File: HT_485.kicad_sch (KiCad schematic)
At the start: 80 parts, among them J1 POWER, J2 485, J3 PT1000, J4 H/T Sensor, J5 PRG, Q1 BC817, Q2 BC817, Q3 BC817, Q4 BC817, U1 MAX14786EAUD+T, U2 TL082, U3 LM2576D2TR4-3.3G, U4 ESP32-S3-WROOM-1-N16R8, U6 L7815

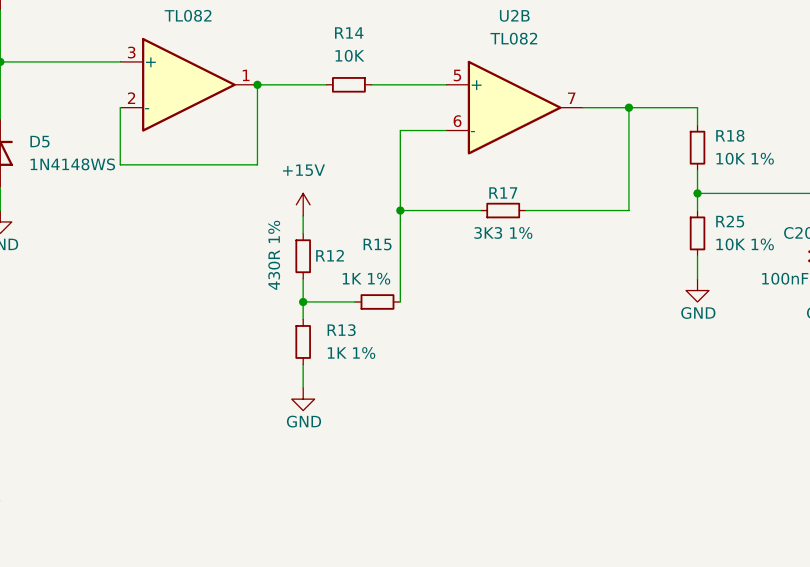
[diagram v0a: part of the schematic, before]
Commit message: Provato cambio resistenze operazionali. NULLA
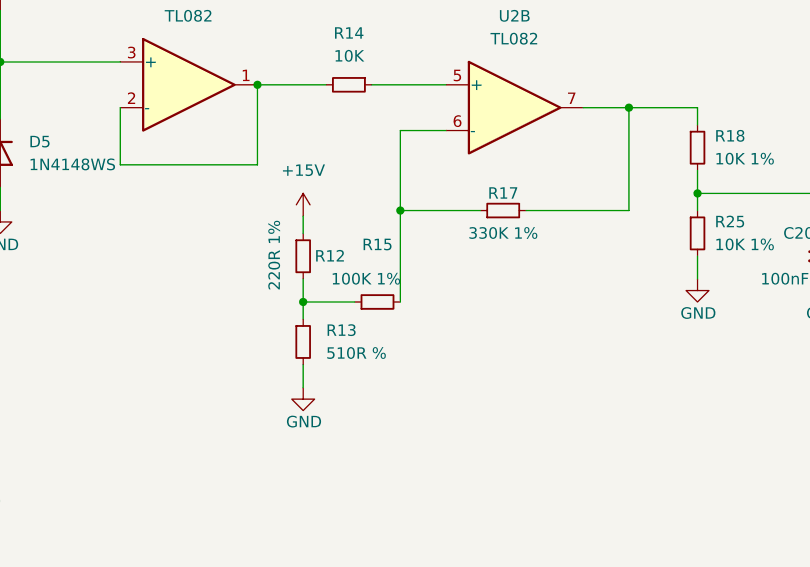
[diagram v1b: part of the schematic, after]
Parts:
- R12: value 430R 1% -> 220R 1%
- R13: value 1K 1% -> 510R %
- R15: value 1K 1% -> 100K 1%
- R17: value 3K3 1% -> 330K 1%
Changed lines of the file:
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@@
     (in_bom yes) (on_board yes)
     (property "Reference" "R17" (id 0) (at 109.855 201.295 90))
-    (property "Value" "3K3 1%" (id 1) (at 109.855 205.74 90))
+    (property "Value" "330K 1%" (id 1) (at 109.855 205.74 90))
     (property "Footprint" "Resistor_SMD:R_0805_2012Metric_Pad1.20x1.40mm_HandSolder" (id 2) (at 109.855 203.2 0)
       (effects (font (size 1.27 1.27)) hide)
@@
       (effects (font (size 1.27 1.27)) (justify left))
     )
-    (property "Value" "430R 1%" (id 1) (at 84.455 212.09 90)
+    (property "Value" "220R 1%" (id 1) (at 84.455 212.09 90)
       (effects (font (size 1.27 1.27)) (justify left))
     )
@@
       (effects (font (size 1.27 1.27)) (justify left))
     )
-    (property "Value" "1K 1%" (id 1) (at 90.17 219.0749 0)
+    (property "Value" "510R %" (id 1) (at 90.17 219.0749 0)
       (effects (font (size 1.27 1.27)) (justify left))
     )
@@
     (in_bom yes) (on_board yes)
     (property "Reference" "R15" (id 0) (at 95.885 207.01 90))
-    (property "Value" "1K 1%" (id 1) (at 94.615 210.82 90))
+    (property "Value" "100K 1%" (id 1) (at 94.615 210.82 90))
     (property "Footprint" "Resistor_SMD:R_0805_2012Metric_Pad1.20x1.40mm_HandSolder" (id 2) (at 95.885 213.36 0)
       (effects (font (size 1.27 1.27)) hide)
@@
     )
     (path "/37a4da1b-b23e-4c99-92c5-1edd1e260509"
-      (reference "R12") (unit 1) (value "430R 1%") (footprint "Resistor_SMD:R_0805_2012Metric_Pad1.20x1.40mm_HandSolder")
+      (reference "R12") (unit 1) (value "220R 1%") (footprint "Resistor_SMD:R_0805_2012Metric_Pad1.20x1.40mm_HandSolder")
     )
     (path "/9b2c5abb-3c78-49d8-8ccb-d7a77fc4039f"
-      (reference "R13") (unit 1) (value "1K 1%") (footprint "Resistor_SMD:R_0805_2012Metric_Pad1.20x1.40mm_HandSolder")
+      (reference "R13") (unit 1) (value "510R %") (footprint "Resistor_SMD:R_0805_2012Metric_Pad1.20x1.40mm_HandSolder")
     )
     (path "/c2ad6d7a-43e9-4769-ab7d-5b48aedd331e"
@@
     )
     (path "/dafc20e6-5160-4991-b11c-f4df07558de3"
-      (reference "R15") (unit 1) (value "1K 1%") (footprint "Resistor_SMD:R_0805_2012Metric_Pad1.20x1.40mm_HandSolder")
+      (reference "R15") (unit 1) (value "100K 1%") (footprint "Resistor_SMD:R_0805_2012Metric_Pad1.20x1.40mm_HandSolder")
     )
     (path "/c722abe2-39f6-4182-8f35-73ac3a447bdd"
@@
     )
     (path "/2ea8c421-e022-4b53-ab9d-747574ed23fe"
-      (reference "R17") (unit 1) (value "3K3 1%") (footprint "Resistor_SMD:R_0805_2012Metric_Pad1.20x1.40mm_HandSolder")
+      (reference "R17") (unit 1) (value "330K 1%") (footprint "Resistor_SMD:R_0805_2012Metric_Pad1.20x1.40mm_HandSolder")
     )
     (path "/7ce32af9-e8f8-4200-8b4f-d83e817f1fc3"

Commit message: Ancora problemi PT1000
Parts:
- R13: value 510R % -> 220R 1%
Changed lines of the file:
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@@
       (effects (font (size 1.27 1.27)) (justify left))
     )
-    (property "Value" "510R %" (id 1) (at 90.17 219.0749 0)
+    (property "Value" "220R 1%" (id 1) (at 90.17 219.0749 0)
       (effects (font (size 1.27 1.27)) (justify left))
     )
@@
     )
     (path "/9b2c5abb-3c78-49d8-8ccb-d7a77fc4039f"
-      (reference "R13") (unit 1) (value "510R %") (footprint "Resistor_SMD:R_0805_2012Metric_Pad1.20x1.40mm_HandSolder")
+      (reference "R13") (unit 1) (value "220R 1%") (footprint "Resistor_SMD:R_0805_2012Metric_Pad1.20x1.40mm_HandSolder")
     )
     (path "/c2ad6d7a-43e9-4769-ab7d-5b48aedd331e"

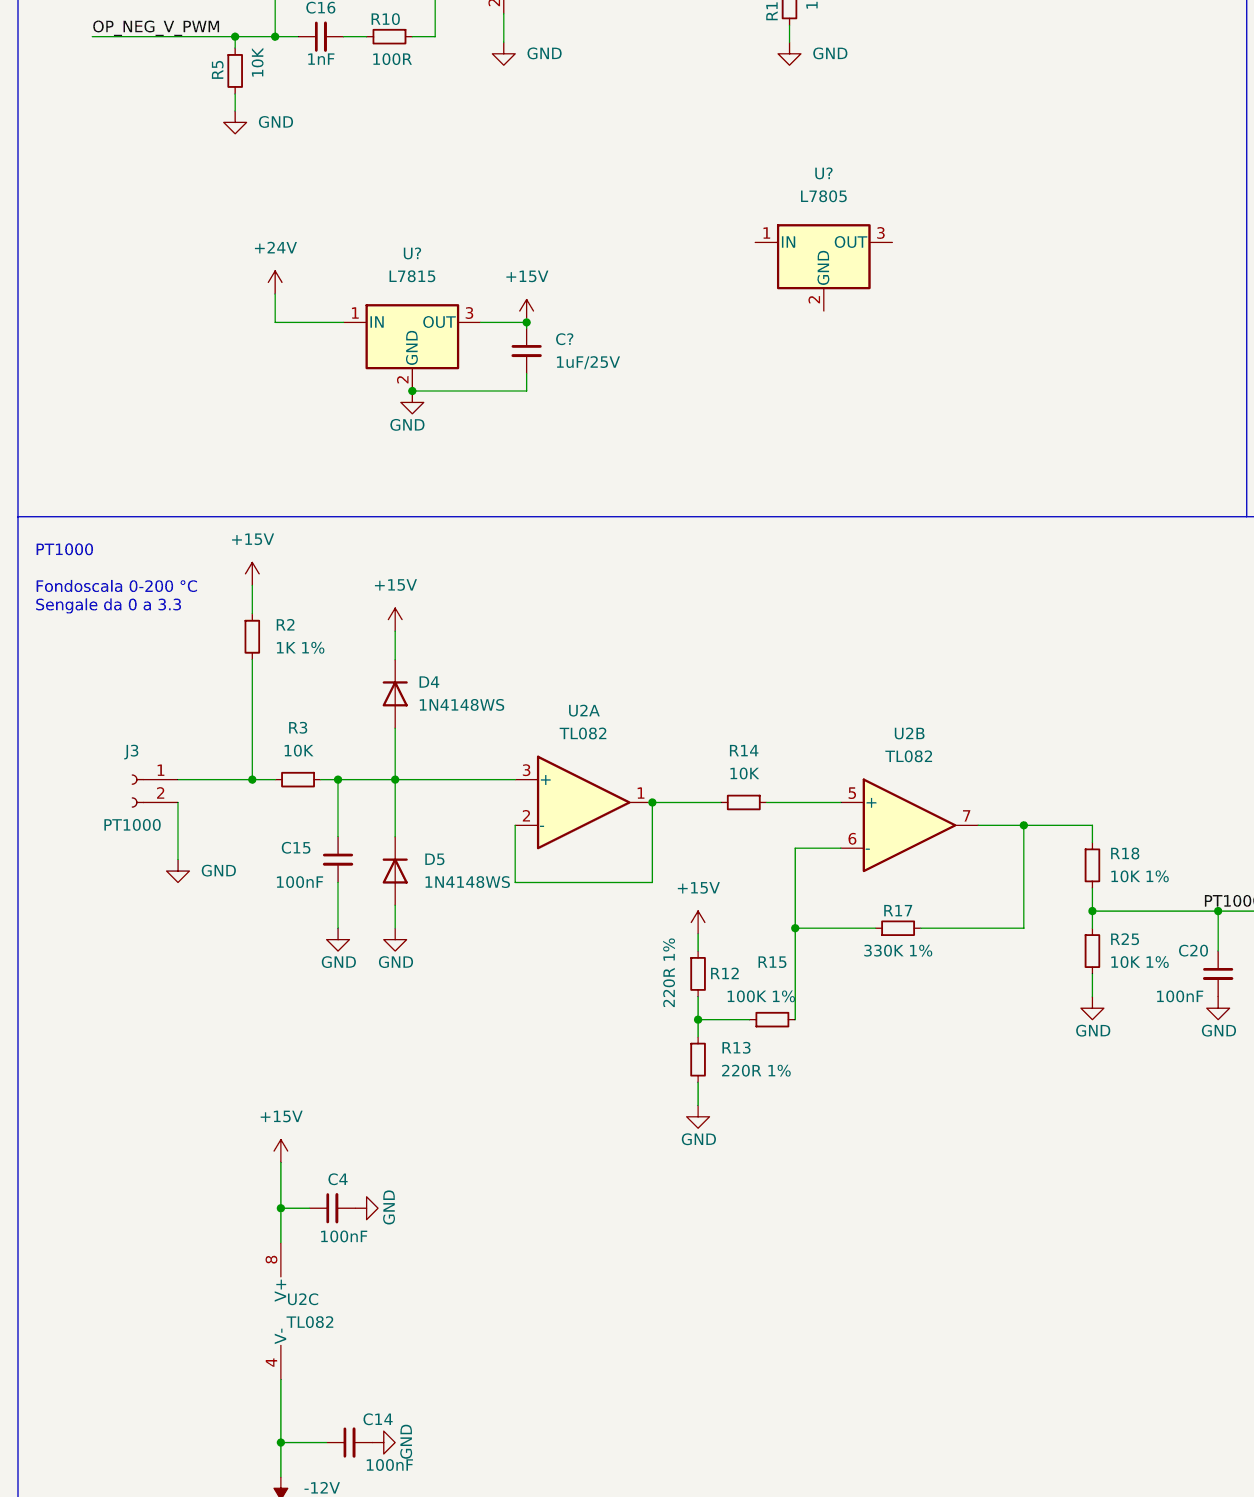
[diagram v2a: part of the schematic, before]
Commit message: Rivisto completamente PT1000 ingresso
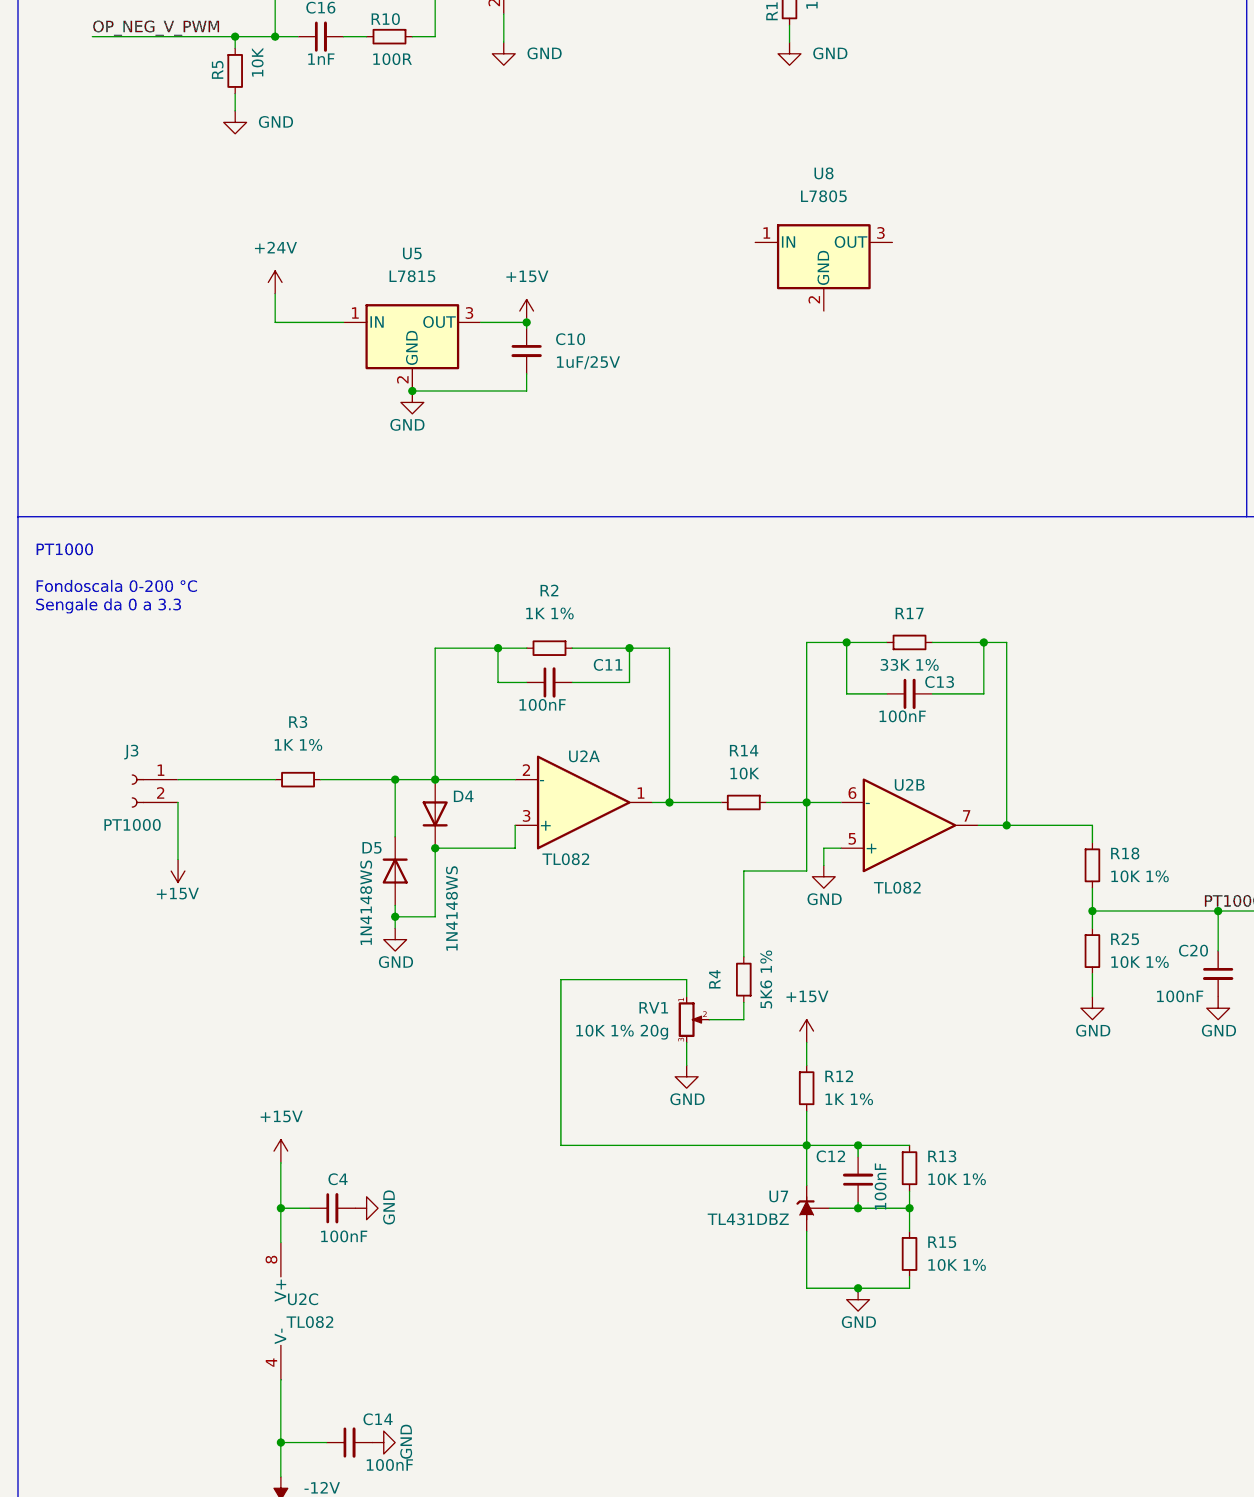
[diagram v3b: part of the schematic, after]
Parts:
- removed C15: 100nF, Capacitor_SMD:C_0805_2012Metric, symbol Device:C_Small
- added C11, C12, C13: 100nF, Capacitor_SMD:C_0805_2012Metric, symbol Device:C_Small
- added R4: 5K6 1%, Resistor_SMD:R_0805_2012Metric_Pad1.20x1.40mm_HandSolder, symbol Device:R_Small
- added RV1: 10K 1% 20g, symbol Device:R_Potentiometer_Small
- added U7: TL431DBZ, Package_TO_SOT_SMD:SOT-23, symbol Reference_Voltage:TL431DBZ
- R12: value 220R 1% -> 1K 1%
- R13: value 220R 1% -> 10K 1%
- R15: value 100K 1% -> 10K 1%
- R17: value 330K 1% -> 33K 1%
- R3: value 10K -> 1K 1%
- gave numbers to parts that had none: 3
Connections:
- net +15V: now also J3.2 (Pin_2); no longer D4.1 (K), R2.1
- net GND: now also D4.1 (K), R15.2, U2.3 (+), U2.5 (+), RV1.3, U7.3 (A); no longer J3.2 (Pin_2), R13.2
- net at R14.1: now also R17.1, U2.6 (-), C13.1, R4.2; no longer U2.5 (+)
- net at R17.2, R18.1, U2.7: now also C13.2
- net at R12.2, R13.1: now also C12.2, RV1.1, U7.1 (K); no longer R15.1
- net at J3.1 (Pin_1), R3.2: no longer R2.2
- net at R14.2, U2.1: now also R2.1, C11.2; no longer U2.2 (-)
- net at D4.2 (A), D5.1 (K), R3.1: now also R2.2, U2.2 (-), C11.1; no longer U2.3 (+)
- new net: R4.1, RV1.2
- new net: C12.1, R13.2, R15.1, U7.2 (REF)
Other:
- moved on the sheet: D4, R17

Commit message: Rifatto schema 485. Master da rifare
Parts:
- removed C7: 1000uF/10V, Capacitor_SMD:CP_Elec_10x10.5, symbol Device:C_Polarized_Small
- removed D10: STPS0520Z, Diode_SMD:D_SOD-123, symbol Device:D_Schottky_Small
- removed D2: 3.9V/1W, Diode_SMD:D_SMA, symbol Device:D_Zener_Small
- removed JP2: BIAS-, Jumper:SolderJumper-2_P1.3mm_Open_RoundedPad1.0x1.5mm, symbol Jumper:SolderJumper_2_Open
- removed JP4: UART_BOOT_MSG, Jumper:SolderJumper-3_P1.3mm_Bridged12_RoundedPad1.0x1.5mm_NumberLabels, symbol Jumper:SolderJumper_3_Bridged12
- removed U1: MAX14786EAUD+T, Package_SO:SOIC-8_3.9x4.9mm_P1.27mm, symbol Interface_UART:MAX485E
- removed U3: LM2576D2TR4-3.3G, Package_TO_SOT_SMD:TO-263-5_TabPin3, symbol Regulator_Switching:LM2575-3.3BU
- removed U5: L7815, Package_TO_SOT_SMD:TO-263-2, symbol Regulator_Linear:L7815
- removed U8: L7805, Package_TO_SOT_SMD:TO-263-2, symbol Regulator_Linear:L7805
- added C15: 1000uF/25V, Capacitor_THT:CP_Radial_D10.0mm_P2.50mm_P5.00mm, symbol Device:C_Polarized_Small
- added C21: 1uF / 25V, Capacitor_SMD:C_0805_2012Metric, symbol Device:C_Small
- added C22, C23: 4.7uF, Capacitor_SMD:C_0805_2012Metric, symbol Device:C_Small
- added C24, C25: 100nF, Capacitor_SMD:C_0805_2012Metric, symbol Device:C_Small
- added C7: 10uF / 25V, Capacitor_SMD:C_0805_2012Metric, symbol Device:C_Small
- added D10, D11, D12, D13, D14, D2: BAR43SFILM, Package_TO_SOT_SMD:SOT-23, symbol Device:D_Dual_Series_AKC
- added Q10, Q5, Q6, Q7, Q8, Q9: BS170, Package_TO_SOT_SMD:SOT-23, symbol Transistor_FET:BS170
- added R32, R33, R34, R35, R36, R37, R41, R42, R43, R44, R45, R46: 4K7, Resistor_SMD:R_0805_2012Metric_Pad1.20x1.40mm_HandSolder, symbol Device:R_Small
- added R38, R39, R40: 10R, Resistor_SMD:R_0805_2012Metric_Pad1.20x1.40mm_HandSolder, symbol Device:R_Small
- added R47: 120R, Resistor_SMD:R_0805_2012Metric_Pad1.20x1.40mm_HandSolder, symbol Device:R_Small
- added SW1: 485_PWR_1, Connector_PinHeader_2.54mm:PinHeader_1x03_P2.54mm_Vertical, symbol Switch:SW_SPDT
- added SW2: 485_PWR_2, Connector_PinHeader_2.54mm:PinHeader_1x03_P2.54mm_Vertical, symbol Switch:SW_SPDT
- added U1: L7805, Package_TO_SOT_SMD:TO-252-3_TabPin2, symbol Regulator_Linear:L7805
- added U3: LD1086DT33TR, Package_TO_SOT_SMD:TO-252-3_TabPin2, symbol Regulator_Linear:LD1117S33TR_SOT223
- added U5: LM2576S-12/NOPB, Package_TO_SOT_SMD:TO-263-5_TabPin3, symbol Regulator_Switching:LM2575-3.3BU
- added U8, U9: MAX485, Package_SO:SOIC-8_3.9x4.9mm_P1.27mm, symbol Interface_UART:MAX485E
- C1: value 4.7uF -> 10uF / 25V
- C10: value 1uF/25V -> 1nF/25V
- C2: value 100nF -> 10uF / 25V
- C5: value 100uF / 50V -> 100uF/75V; footprint Capacitor_SMD:CP_Elec_8x10.5 -> Capacitor_THT:CP_Radial_D10.0mm_P2.50mm_P5.00mm
- C6: value 1nF/10V -> 10uF / 25V
- J1: value POWER -> 485_1
- J2: value 485 -> 485_1
- JP1: value BIAS+ -> TERMINATOR
- L1: value 100uH -MSS1210-104KED -> MSS1210-104KED -100uH; footprint HT485:MSS1210-104KED -> SES:MSS1210-104KED
- R20: value 370R -> 0R
- R21: value 370R -> 10R
- R23: value 4K7 -> 10R
- R31: value 10K -> 10R
- U4: value ESP32-S3-WROOM-1-N16R8 -> ESP32-S3-WROOM-1U-N16R8
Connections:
- net +15V: no longer C10.1
- net +24V: now also U5.1 (VIN); no longer J1.2 (Pin_2)
- net +3V3: now also C7.1, D10.2 (K), D11.2 (K), D12.2 (K), D13.2 (K), D14.2 (K), D2.2 (K), Q10.2 (G), Q5.2 (G), Q6.2 (G), Q7.2 (G), Q8.2 (G), Q9.2 (G), R32.2, R33.2, R34.2, R41.2, R42.2, R43.2, U3.2 (VO); no longer L1.2, R20.1, R23.2, R31.1
- net +5V: now also C2.1, C6.1, SW1.3 (C), SW2.3 (C), U1.3 (OUT), U3.3 (VI); no longer C1.2, C2.2
- net GND: now also C1.2, C2.2, R1.1, C15.2, C21.2, C22.1, C23.1, C24.1, C25.1, C7.2, D10.1 (A), D11.1 (A), D12.1 (A), D13.1 (A), D14.1 (A), D2.1 (A), U1.2 (GND), U3.1 (GND), U5.5 (~{ON}/OFF), U8.5 (GND), U9.5 (GND); no longer C1.1, C2.1, J1.1 (Pin_1), R1.2, R21.2
- net at D1.1 (K), L1.1, R6.1: now also U5.2 (OUT)
- net at U4.16 (GPIO46): now also R30.1
- net DE2: now reaches U4.20 (GPIO12/TOUCH11/ADC2_CH0/FSPICS0/FSPIIO4/SUBSPICS0)
- net DE2: now also D14.3 (common), R40.2
- net TX2: now reaches U4.21 (GPIO13/TOUCH13/ADC2_CH2/FSPIQ/FSPIIO7/SUBSPIQ)
- net TX2: now also D13.3 (common), R39.2
- net RX2: now reaches U4.22 (GPIO14/TOUCH14/ADC2_CH3/FSPIWP/FSPIDQS/SUBSPIWP)
- net RX2: now also D12.3 (common), R38.2
- net DE1: now reaches U4.9 (GPIO16/U0CTS/ADC2_CH5/XTAL_32K_NH5)
- net DE1: now also R31.2, D11.3 (common)
- net at R6.2: now also C10.1; no longer C6.1
- net +12V: now reaches R20.2
- net +12V: now also C1.1, L1.2, C15.1, C21.1, SW1.1 (A), SW2.1 (A), U1.1 (IN); no longer JP1.2 (B)
- net at R21.1: now also Q5.3 (S), R32.1
- net 485+ renamed 485_1+
- net 485_1+: now also U9.7 (B); no longer JP1.1 (A)
- net 485- renamed 485_1-
- net 485_1-: now also U9.6 (A)
- net DE: no longer names the net of U4.4 (GPIO4/TOUCH4/ADC1_CH3)
- net DE: no longer R1.1
- net RX: no longer names the net of R23.1
- net RX: now also Q6.3 (S), R33.1; no longer U4.11 (GPIO18/U1RXD/ADC2_CH7/CLK_OUT3)
- net TX renamed TX1
- net TX1: now also R23.2, D10.3 (common)
- new net: Q8.3 (S), R38.1, R41.1
- new net: Q9.3 (S), R39.1, R42.1
- new net: Q10.3 (S), R40.1, R43.1
- new net: Q7.3 (S), R31.1, R34.1
- new net: JP1.1 (A), R47.1
- new net: R1.2, R20.1, U5.4 (FB)
- new net 485_2+: J1.2 (Pin_2), JP1.2 (B), U8.7 (B)
- new net 485_2-: J1.1 (Pin_1), R47.2, U8.6 (A)
- new net DEH1: Q7.1 (D), R37.1, U9.2 (~{RE}), U9.3 (DE)
- new net DEH2: Q10.1 (D), R46.1, U8.2 (~{RE}), U8.3 (DE)
- new net RX1: D2.3 (common), R21.2, U4.11 (GPIO18/U1RXD/ADC2_CH7/CLK_OUT3)
- new net RXH1: Q5.1 (D), R35.1, U9.1 (RO)
- new net RXH2: Q8.1 (D), R44.1, U8.1 (RO)
- new net TXH1: Q6.1 (D), R36.1, U9.4 (DI)
- new net TXH2: Q9.1 (D), R45.1, U8.4 (DI)
- new net VCC1: C23.2, C25.2, R35.2, R36.2, R37.2, SW1.2 (B), U9.8 (VCC)
- new net VCC2: C22.2, C24.2, R44.2, R45.2, R46.2, SW2.2 (B), U8.8 (VCC)
- no-connect marks 21 -> 17
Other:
- note added: "Se LM7576-12 non motare R2"
- moved on the sheet: C11, C12, C13, C14, C16, C17, C18, C19, C20, C3, C4, C8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

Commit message: Rivisto tutta la scheda
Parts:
- removed C1, C2: 10uF / 25V, Capacitor_SMD:C_0805_2012Metric, symbol Device:C_Small
- removed C17: 1uF/25V, Capacitor_SMD:C_0805_2012Metric, symbol Device:C_Small
- removed TP1: D+, TestPoint:TestPoint_Pad_D1.0mm, symbol Connector:TestPoint
- removed TP2: D-, TestPoint:TestPoint_Pad_D1.0mm, symbol Connector:TestPoint
- removed U6: L7815, Package_TO_SOT_SMD:TO-263-2, symbol Regulator_Linear:L7815
- added D15: VSSAF522-M3/H, Diode_SMD:D_SMA-SMB_Universal_Handsoldering, symbol Device:D_Schottky_Small
- added J6: PWR, TerminalBlock_Phoenix:TerminalBlock_Phoenix_PT-1,5-2-3.5-H_1x02_P3.50mm_Horizontal, symbol Connector:Conn_01x02_Female
- C15: footprint Capacitor_THT:CP_Radial_D10.0mm_P2.50mm_P5.00mm -> Capacitor_SMD:CP_Elec_10x10.5
- C5: footprint Capacitor_THT:CP_Radial_D10.0mm_P2.50mm_P5.00mm -> Capacitor_SMD:CP_Elec_8x10.5
- L1: footprint SES:MSS1210-104KED -> HT485:MSS1210-104KED
- RV1: value 10K 1% 20g -> 10K 1% 20g -3296Y-1-103LF; footprint (none) -> Potentiometer_THT:Potentiometer_Bourns_3296Y_Vertical
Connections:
- net +15V is gone; now on net +12V: C4.1, J3.2 (Pin_2), Q2.3 (C), R11.1, R12.1, U2.8 (V+)
- net +24V: now also D15.1 (K)
- net ALERT: now also U4.35 (MTMS/GPIO42); no longer U4.15 (GPIO3/TOUCH3/ADC1_CH2)
- net DE1: now also U4.18 (GPIO10/TOUCH10/ADC1_CH9/FSPICS0/FSPIIO4/SUBSPICS0); no longer U4.9 (GPIO16/U0CTS/ADC2_CH5/XTAL_32K_NH5)
- net DE2: now also U4.21 (GPIO13/TOUCH13/ADC2_CH2/FSPIQ/FSPIIO7/SUBSPIQ); no longer U4.20 (GPIO12/TOUCH11/ADC2_CH0/FSPICS0/FSPIIO4/SUBSPICS0)
- net GND: now also U5.3 (GND), J6.2 (Pin_2)
- net OP_NEG_V_PWM: now also U4.32 (MTCK/GPIO39/CLK_OUT3/SUBSPICS1); no longer U4.5 (GPIO5/TOUCH5/ADC1_CH4)
- net RX1: now also U4.17 (GPIO9/TOUCH9/ADC1_CH8/FSPIHD/SUBSPIHD); no longer U4.11 (GPIO18/U1RXD/ADC2_CH7/CLK_OUT3)
- net SCL: now also U4.34 (MTDI/GPIO41/CLK_OUT1); no longer U4.25 (GPIO48/SPICLK_N/SUBSPICLK_N_DIFF)
- net SDA: now also U4.33 (MTDO/GPIO40/CLK_OUT2); no longer U4.24 (GPIO47/SPICLK_P/SUBSPICLK_P_DIFF)
- net TX1: now also U4.15 (GPIO3/TOUCH3/ADC1_CH2); no longer U4.10 (GPIO17/U1TXD/ADC2_CH6)
- net TX2: now also U4.20 (GPIO12/TOUCH11/ADC2_CH0/FSPICS0/FSPIIO4/SUBSPICS0); no longer U4.21 (GPIO13/TOUCH13/ADC2_CH2/FSPIQ/FSPIIO7/SUBSPIQ)
- net D+: no longer names the net of U4.14 (GPIO20/U1CTS/ADC2_CH9/CLK_OUT1/USB_D+)
- net D-: no longer names the net of U4.13 (GPIO19/U1RTS/ADC2_CH8/CLK_OUT2/USB_D-)
- new net: D15.2 (A), J6.1 (Pin_1)
- no-connect marks 17 -> 13
